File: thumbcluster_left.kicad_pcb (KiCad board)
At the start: 2 copper layers, 63.6 x 37.8 mm, 12 parts, among them J1 Conn_01x06_Female, J2 Conn_01x06_Female, SW1 SW_Push, SW2 SW_Push, SW3 SW_Push, SW4 SW_Push, SW5 SW_Push

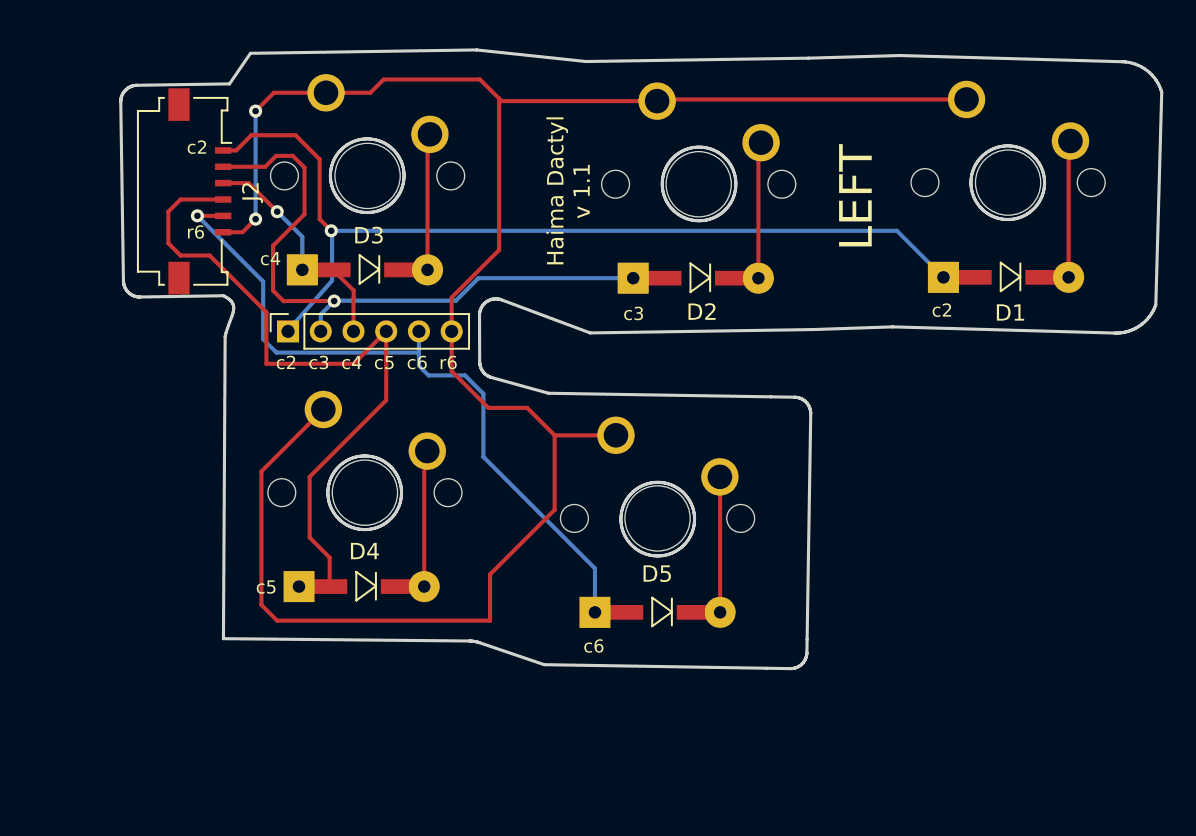
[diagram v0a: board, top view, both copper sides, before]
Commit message: Complete net refactor
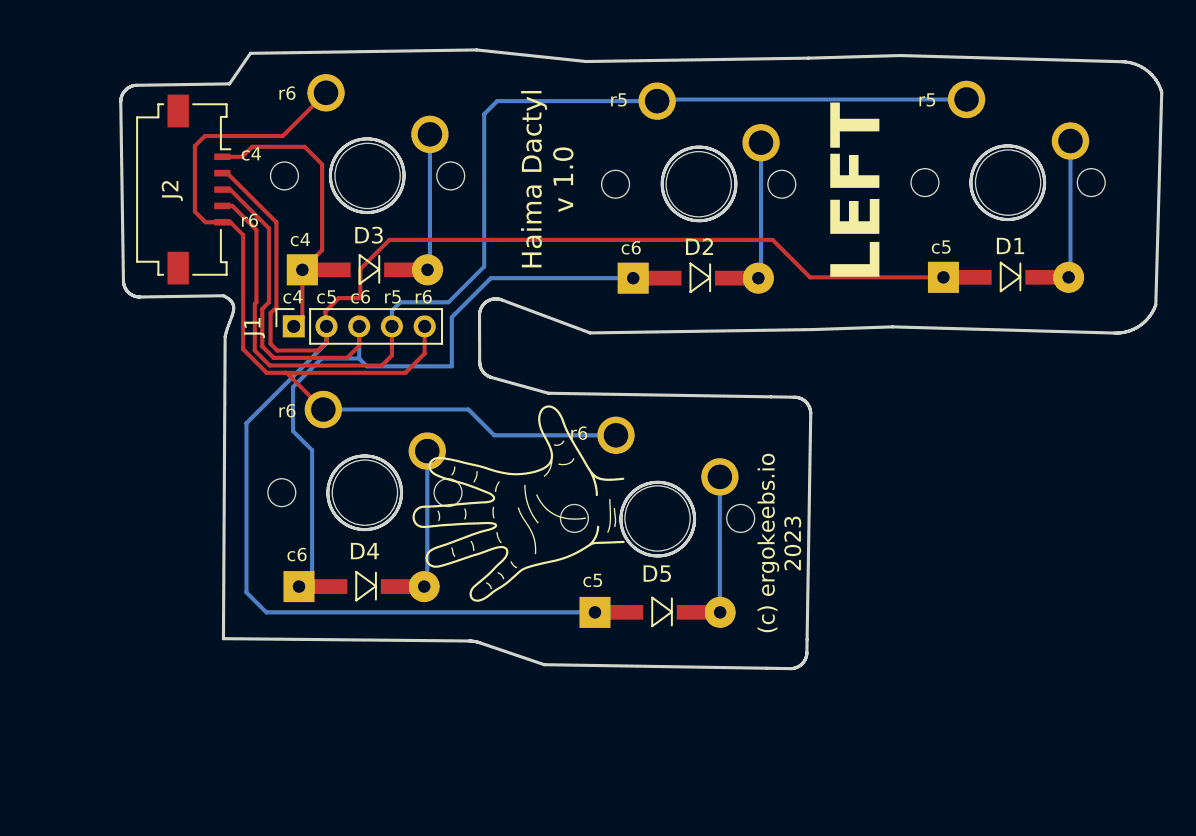
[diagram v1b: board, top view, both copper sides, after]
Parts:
- J1: value Conn_01x06_Female -> Thumb; footprint Connector_PinSocket_2.00mm:PinSocket_1x06_P2.00mm_Vertical -> Connector_PinSocket_2.00mm:PinSocket_1x05_P2.00mm_Vertical
- J2: value Conn_01x06_Female -> Thumb; footprint Connector_FFC-FPC:Molex_200528-0060_1x06-1MP_P1.00mm_Horizontal -> Connector_FFC-FPC:Molex_200528-0050_1x05-1MP_P1.00mm_Horizontal
- moved J1 0.46 mm to (36.4, 137.6)
- moved J2 0.12 mm to (31.1, 129.2)
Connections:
- D1 pad 1: col2 -> col5
- D2 pad 1: col3 -> col6
- D4 pad 1: col5 -> col6
- D5 pad 1: col6 -> col5
- J1 pad 1: col2 -> col4
- J1 pad 2: col3 -> col5
- J1 pad 3: col4 -> col6
- J1 pad 4: col5 -> row5
- J1 pad 5: col6 -> row6
- J2 pad 1: col2 -> col4
- J2 pad 2: col3 -> col5
- J2 pad 3: col4 -> col6
- J2 pad 4: col5 -> row5
- J2 pad 5: col6 -> row6
- SW1 pad 1: row6 -> row5
- SW2 pad 1: row6 -> row5
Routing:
- net row5: track 0.00 -> 67.8 mm
- net row6: track 124.1 -> 59.6 mm, vias 2 -> 0
- net col2: track 57.3 -> 0.00 mm, vias 1 -> 0
- net col5: track 42.7 -> 99.5 mm
- net col3: track 38.9 -> 0.00 mm, vias 1 -> 0
- net col6: track 43.6 -> 59.6 mm, vias 1 -> 0
- net col4: track 12.5 -> 17.4 mm, vias 1 -> 0
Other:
- board text added: "(c) ergokeebs.io 2023"
- board text added: "Haima Dactyl v 1.0"
- board text added: "r5"
- board text removed: "Haima Dactyl v 1.1"
- board text removed: "c2"
- board text removed: "c3"

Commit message: Routing
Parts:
- moved J2 52.6 mm to (83.7, 129.1), turned to 90 degrees
- moved D1 44.8 mm to (31.3, 134.5)
- moved SW1 44.8 mm to (35.2, 128.8)
- moved J1 42.1 mm to (78.5, 138.5), turned to -90 degrees
- moved D4 33.8 mm to (70.5, 153.4)
- moved SW4 33.8 mm to (74.5, 147.7)
- moved D3 33.5 mm to (70.4, 134.0)
- moved SW3 33.5 mm to (74.4, 128.3)
- moved D2 7.06 mm to (50.1, 134.5)
- moved SW2 7.06 mm to (54.1, 128.8)
- moved SW5 1.98 mm to (56.6, 149.4)
- moved D5 1.98 mm to (52.8, 155.0)
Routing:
- net col5: track 99.5 -> 123.2 mm
- net row5: track 67.8 -> 79.1 mm, vias 0 -> 1
- net col4: track 17.4 -> 23.3 mm
- net row6: track 59.6 -> 57.3 mm, vias 0 -> 1
- net col6: track 59.6 -> 57.5 mm
- net Net-(D5-A): track 8.29 -> 8.94 mm
- net Net-(D3-A): track 8.34 -> 8.89 mm
- net Net-(D2-A): track 8.35 -> 8.89 mm
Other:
- outline, holes or cut-outs redrawn
- board text added: "Haima Dactyl v 1.3"
- board text added: "RIGHT"
- board text removed: "Haima Dactyl v 1.0"
- board text removed: "LEFT"
